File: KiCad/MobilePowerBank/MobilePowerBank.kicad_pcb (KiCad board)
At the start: 2 copper layers, 114 x 164 mm, 123 parts, among them J1 Power IN, J2 Power OUT, J3 Power OUT, J4 OLED I2C, J5 PDI, J6 OLED, J7 Power OUT, SW1 SW_DIP_x01, U1 INA169, U10 INA138, U2 LMZ14203H, U3 L78M12, U4 INA138, U5 UA78M33, U6 ATXMEGA32E5-AU, U7 LMZ14203H, U8 LMZ14203H, U9 INA138

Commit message: 5 power supplies created
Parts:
- removed the REF** at (134.6, 29.8)
- removed the REF** at (52.1, 29.8)
- added C45: 100u, Capacitors_Tantalum_SMD:CP_Tantalum_Case-V_EIA-7343-20_Wave, F.Cu at (46.4, 101.0)
- added C46: 100u, Capacitors_Tantalum_SMD:CP_Tantalum_Case-V_EIA-7343-20_Wave, F.Cu at (102.9, 101.0)
- added C47: 10u/35V/X7R, Capacitors_SMD:C_2220, F.Cu at (52.7, 101.0)
- added C48: 10u/35V/X7R, Capacitors_SMD:C_2220, F.Cu at (109.2, 101.0)
- added C49: 4u7, Capacitors_SMD:C_0805, F.Cu at (62.9, 109.2)
- added C50: 4u7, Capacitors_SMD:C_0805, F.Cu at (119.4, 109.2)
- added C51: 22n, Capacitors_SMD:C_0805, F.Cu at (70.5, 108.0)
- added C52: 22n, Capacitors_SMD:C_0805, F.Cu at (127.0, 108.0)
- added C53: 47u/1-45mESR, Capacitors_Tantalum_SMD:CP_Tantalum_Case-D_EIA-7343-31_Reflow, F.Cu at (70.5, 101.0)
- added C54: 47u/1-45mESR, Capacitors_Tantalum_SMD:CP_Tantalum_Case-D_EIA-7343-31_Reflow, F.Cu at (127.0, 101.0)
- added C55: 47u/1-45mESR, Capacitors_Tantalum_SMD:CP_Tantalum_Case-D_EIA-7343-31_Reflow, F.Cu at (76.2, 101.0)
- added C56: 47u/1-45mESR, Capacitors_Tantalum_SMD:CP_Tantalum_Case-D_EIA-7343-31_Reflow, F.Cu at (132.7, 101.0)
- added C57: 100n, Capacitors_SMD:C_0805, F.Cu at (8.87, 104.5)
- added C58: 100n, Capacitors_SMD:C_0805, F.Cu at (8.87, 100.8)
- added C59: 100n, Capacitors_SMD:C_0805, B.Cu at (80.0, 108.6)
- added C60: 100n, Capacitors_SMD:C_0805, B.Cu at (136.5, 108.6)
- added C61: 1u, Capacitors_SMD:C_0805, F.Cu at (25.6, 91.6)
- added C62: 1u, Capacitors_SMD:C_0805, F.Cu at (8.87, 102.6)
- added J8: Power OUT 4, Connectors_Terminal_Blocks:TerminalBlock_Altech_AK300-2_P5.00mm, F.Cu at (93.3, 103.5)
- added J9: Power OUT 5, Connectors_Terminal_Blocks:TerminalBlock_Altech_AK300-2_P5.00mm, F.Cu at (149.9, 103.5)
- added R56: 220k, Resistors_SMD:R_0805, F.Cu at (54.6, 108.6)
- added R57: 30k, Resistors_SMD:R_0805, F.Cu at (54.6, 110.5)
- added R58: 220k, Resistors_SMD:R_0805, F.Cu at (111.1, 108.6)
- added R59: 30k, Resistors_SMD:R_0805, F.Cu at (111.1, 110.5)
- added R60: 30k, Resistors_SMD:R_0805, F.Cu at (57.8, 108.6)
- added R61: 300k, Resistors_SMD:R_0805, F.Cu at (57.8, 110.5)
- added R62: 30k, Resistors_SMD:R_0805, F.Cu at (114.3, 108.6)
- added R63: 300k, Resistors_SMD:R_0805, F.Cu at (114.3, 110.5)
- added R64: 20k, Resistors_SMD:R_0805, F.Cu at (61.0, 111.1)
- added R65: 20k, Resistors_SMD:R_0805, F.Cu at (117.5, 111.1)
- added R66: 2k2, Resistors_SMD:R_0805, F.Cu at (66.0, 109.2)
- added R67: 2k2, Resistors_SMD:R_0805, F.Cu at (122.6, 109.2)
- added R68: 15k4, Resistors_SMD:R_0805, F.Cu at (67.9, 109.2)
- added R69: 15k4, Resistors_SMD:R_0805, F.Cu at (124.5, 109.2)
- added R70: 15k4, Resistors_SMD:R_0805, F.Cu at (70.5, 109.9)
- added R71: 15k4, Resistors_SMD:R_0805, F.Cu at (127.0, 109.9)
- added R72: 90k, Resistors_SMD:R_0805, F.Cu at (11.8, 108.2)
- added R73: 10k, Resistors_SMD:R_0805, F.Cu at (15.4, 104.5)
- added R74: 90k, Resistors_SMD:R_0805, F.Cu at (28.9, 91.6)
- added R75: 10k, Resistors_SMD:R_0805, F.Cu at (22.0, 95.8)
- added R76: 0R1, Resistors_SMD:R_2512, F.Cu at (83.2, 103.5)
- added R77: 0R1, Resistors_SMD:R_2512, F.Cu at (83.2, 107.3)
- added R78: 0R1, Resistors_SMD:R_2512, F.Cu at (83.2, 111.1)
- added R79: 0R1, Resistors_SMD:R_2512, F.Cu at (139.7, 103.5)
- added R80: 0R1, Resistors_SMD:R_2512, F.Cu at (139.7, 107.3)
- added R81: 0R1, Resistors_SMD:R_2512, F.Cu at (139.7, 111.1)
- added R82: 20k, Resistors_SMD:R_0805, B.Cu at (81.3, 111.8)
- added R83: 20k, Resistors_SMD:R_0805, B.Cu at (137.8, 111.8)
- added REF**: MountingHole_3.2mm_M3, Mounting_Holes:MountingHole_3.2mm_M3, F.Cu at (148.5, 188.5)
- added REF**: MountingHole_3.2mm_M3, Mounting_Holes:MountingHole_3.2mm_M3, F.Cu at (45.5, 188.5)
- added REF**: MountingHole_3.2mm_M3, Mounting_Holes:MountingHole_3.2mm_M3, F.Cu at (148.5, 55.5)
- added REF**: MountingHole_3.2mm_M3, Mounting_Holes:MountingHole_3.2mm_M3, F.Cu at (45.5, 55.5)
- added U11: LMZ14201H, TO_SOT_Packages_SMD:TO-263-7_TabPin4, F.Cu at (61.6, 98.4)
- added U12: LMZ14201H, TO_SOT_Packages_SMD:TO-263-7_TabPin4, F.Cu at (118.1, 98.4)
- added U13: INA138, TO_SOT_Packages_SMD:SOT-23-5, B.Cu at (83.2, 109.2)
- added U14: INA138, TO_SOT_Packages_SMD:SOT-23-5, B.Cu at (139.7, 109.2)
- added U15: ATXMEGA256A3U-AU, Housings_QFP:TQFP-64_14x14mm_Pitch0.8mm, B.Cu at (101.0, 31.1)
- J2: value Power OUT -> Power OUT 2
- J3: value Power OUT -> Power OUT 1
- J7: value Power OUT -> Power OUT 3
- moved REF** 148.0 mm to (236.1, 117.9)
- moved C27 143.3 mm to (179.1, 42.5)
- moved R24 114.3 mm to (132.1, 55.9), turned to 0 degrees
- moved C15 105.4 mm to (93.3, 50.8)
- moved C18 105.4 mm to (99.1, 66.7)
- moved C19 105.4 mm to (98.4, 66.7)
- moved C21 105.4 mm to (88.3, 56.5)
- moved C26 105.4 mm to (95.9, 50.8)
- moved L1 105.4 mm to (84.5, 56.5)
- moved R1 105.4 mm to (89.5, 50.8)
- moved R12 105.4 mm to (99.7, 50.8)
- moved R13 105.4 mm to (97.8, 50.8)
- moved R2 105.4 mm to (91.4, 50.8)
- moved U3 105.4 mm to (73.0, 56.5)
- moved C12 105.4 mm to (129.5, 48.3)
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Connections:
- C26 pad 1: OUT_Voltage -> OUT_1_Voltage
- C27 pad 1: OUT_Current -> OUT_1_Current
- C39 pad 1: OUT_Voltage -> OUT_2_Voltage
- C40 pad 1: OUT_Voltage -> OUT_3_Voltage
- C43 pad 1: OUT_Current -> OUT_2_Current
- C44 pad 1: OUT_Current -> OUT_3_Current
- R12 pad 2: OUT_Voltage -> OUT_1_Voltage
- R13 pad 1: OUT_Voltage -> OUT_1_Voltage
- R15 pad 1: OUT_Current -> OUT_1_Current
- R44 pad 2: OUT_Voltage -> OUT_2_Voltage
- R45 pad 1: OUT_Voltage -> OUT_2_Voltage
- R46 pad 2: OUT_Voltage -> OUT_3_Voltage
- R47 pad 1: OUT_Voltage -> OUT_3_Voltage
- R54 pad 1: OUT_Current -> OUT_2_Current
- R55 pad 1: OUT_Current -> OUT_3_Current
- U10 pad 1: OUT_Current -> OUT_3_Current
- U4 pad 1: OUT_Current -> OUT_1_Current
- U6 pad 5: OUT_Voltage -> (no net)
- U6 pad 6: OUT_Current -> (no net)
- U9 pad 1: OUT_Current -> OUT_2_Current
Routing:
- net GNDA: track 198.0 -> 309.8 mm
- net POWER_IN: track 165.2 -> 120.5 mm
- net OUT_Current: track 41.5 -> 0.00 mm, vias 1 -> 0
- net Net-(C52-Pad1): track 0.00 -> 29.5 mm
- net Net-(C51-Pad1): track 0.00 -> 28.5 mm
- net IN_Current: track 38.8 -> 11.1 mm
- net PDI_CLK: track 44.0 -> 17.6 mm
- net PDI_DATA: track 41.7 -> 22.7 mm
- net Net-(C10-Pad1): track 65.5 -> 48.5 mm
- net GND: track 275.4 -> 258.5 mm, vias 9 -> 8
- net (no net): track 1.90 -> 17.7 mm, vias 0 -> 1
- net Net-(F1-Pad1): track 15.0 -> 0.00 mm
- net Net-(C52-Pad2): track 0.00 -> 8.61 mm
- net Net-(C51-Pad2): track 0.00 -> 8.61 mm
- net Net-(R63-Pad2): track 0.00 -> 8.31 mm
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- added copper zone on F.Cu, net Net-(C51-Pad1)
- added copper zone on F.Cu, net Net-(C52-Pad1)
- added copper zone on F.Cu, net POWER_4_OUT
- added copper zone on F.Cu, net POWER_5_OUT
- removed copper zone on B.Cu, net Net-(F1-Pad1)
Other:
- board text removed: "In(35V)"
- board text removed: "Out"
- board text removed: "Vin"
- board text removed: "Vout"

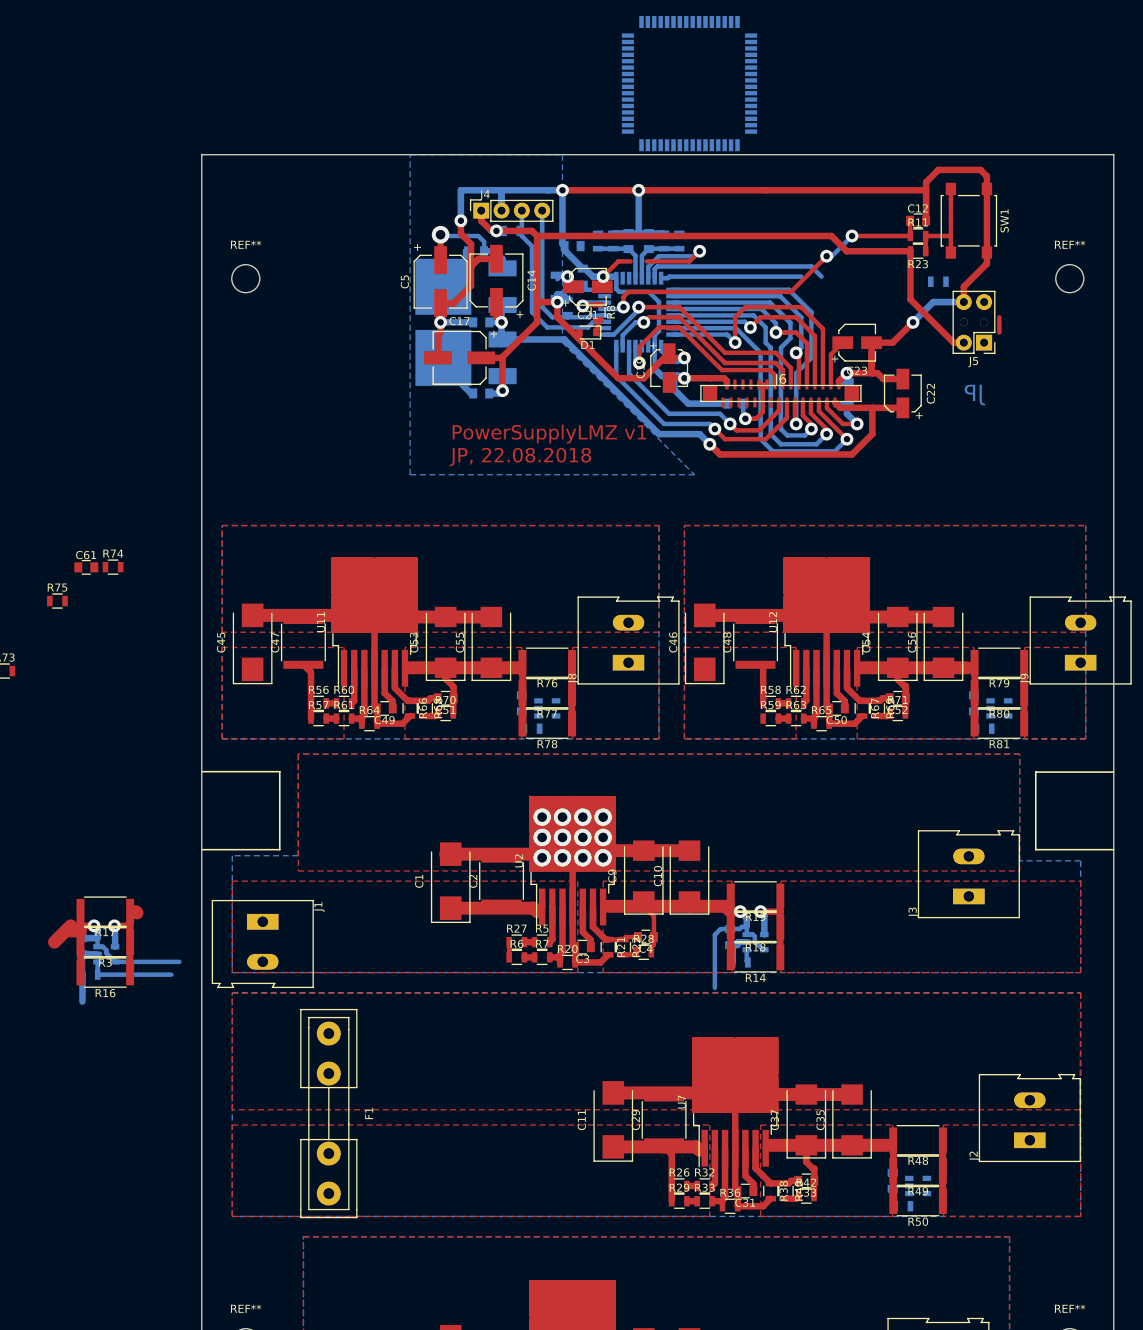
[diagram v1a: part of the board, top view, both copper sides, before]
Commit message: xmega added
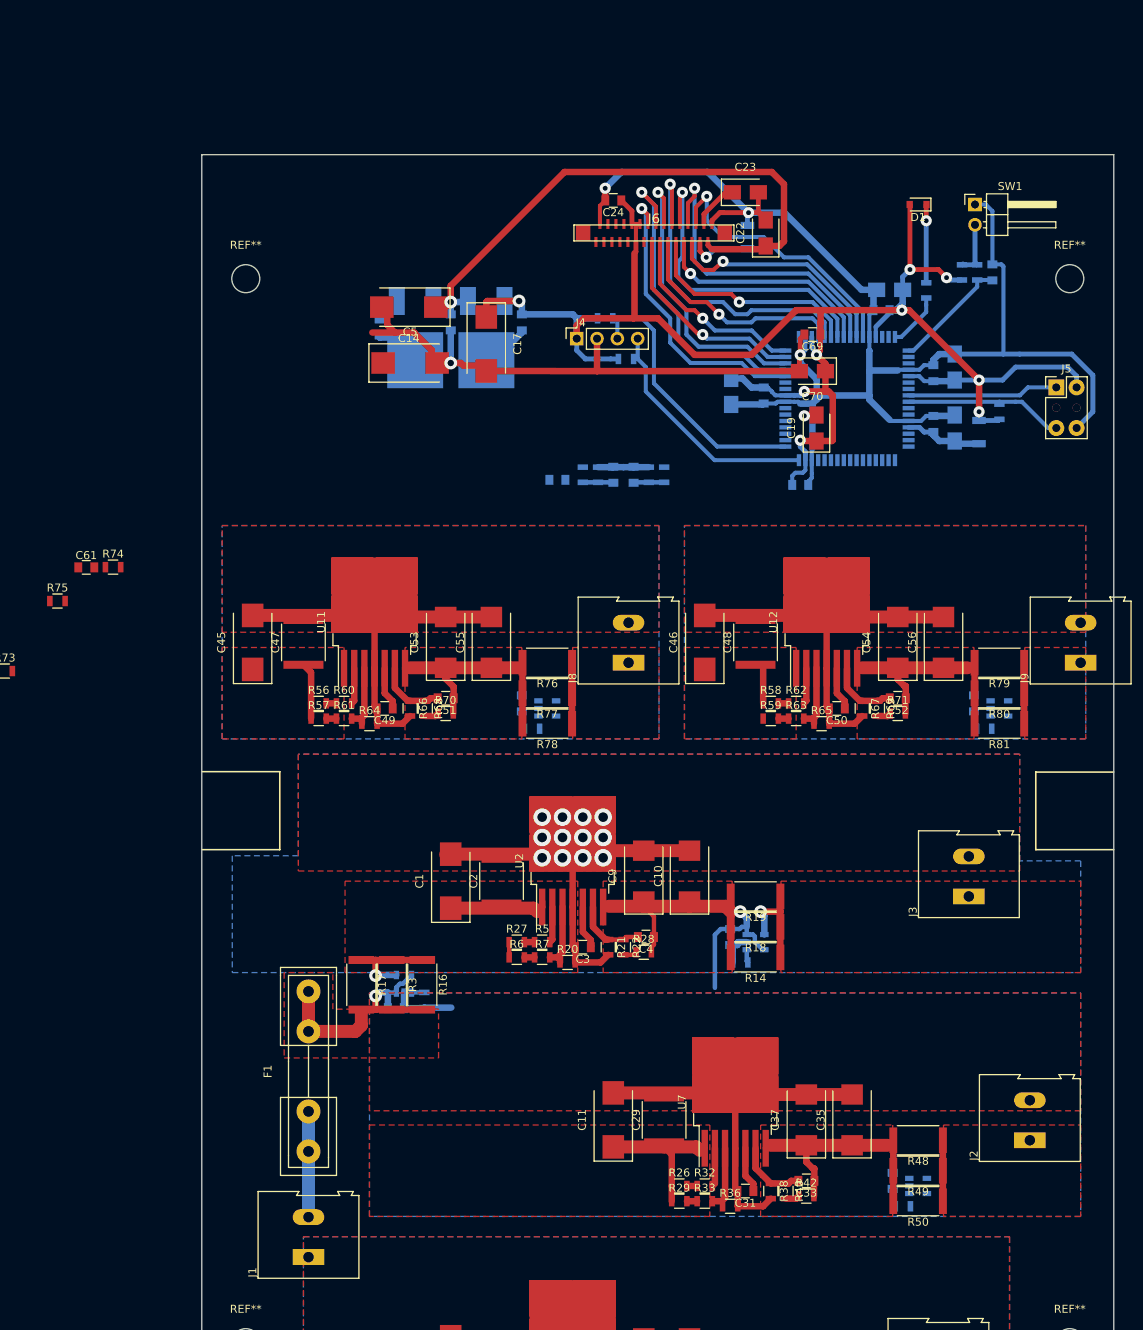
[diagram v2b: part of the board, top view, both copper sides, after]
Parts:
- removed U6: ATXMEGA32E5-AU, Housings_QFP:TQFP-32_7x7mm_Pitch0.8mm
- added C63: 100n, Capacitors_SMD:C_0805, B.Cu at (125.0, 59.4)
- added C64: 10u, Capacitors_Tantalum_SMD:CP_Tantalum_Case-B_EIA-3528-21_Wave, B.Cu at (126.0, 56.9)
- added C65: 100n, Capacitors_SMD:C_0805, B.Cu at (131.4, 67.3)
- added C66: 10u, Capacitors_Tantalum_SMD:CP_Tantalum_Case-B_EIA-3528-21_Wave, B.Cu at (134.1, 66.5)
- added C67: 100n, Capacitors_SMD:C_0805, B.Cu at (110.2, 70.1)
- added C68: 10u, Capacitors_Tantalum_SMD:CP_Tantalum_Case-B_EIA-3528-21_Wave, B.Cu at (106.2, 69.6)
- added C69: 100n, Capacitors_SMD:C_0805, F.Cu at (116.3, 62.5)
- added C70: 10u, Capacitors_Tantalum_SMD:CP_Tantalum_Case-B_EIA-3528-21_Wave, F.Cu at (116.3, 67.1)
- C1, C11, C28, C45, C46: value 100u -> 47u
- C12, R11, R23, R8: moved to B.Cu
- C13: value 100n -> 47u
- C14: footprint Capacitors_SMD:CP_Elec_6.3x7.7 -> Capacitors_Tantalum_SMD:CP_Tantalum_Case-V_EIA-7343-20_Wave
- C17: footprint Capacitors_SMD:CP_Elec_6.3x5.8 -> Capacitors_Tantalum_SMD:CP_Tantalum_Case-V_EIA-7343-20_Wave
- C19, C22, C23: footprint Capacitors_SMD:CP_Elec_4x5.8 -> Capacitors_Tantalum_SMD:CP_Tantalum_Case-B_EIA-3528-21_Wave
- C21: footprint Capacitors_SMD:CP_Elec_4x5.8 -> Capacitors_Tantalum_SMD:CP_Tantalum_Case-B_EIA-3528-21_Wave; moved to B.Cu
- C24: moved to F.Cu
- C5: value 100u -> 47u; footprint Capacitors_SMD:CP_Elec_6.3x7.7 -> Capacitors_Tantalum_SMD:CP_Tantalum_Case-V_EIA-7343-20_Wave
- SW1: footprint Buttons_Switches_SMD:SW_SPST_B3S-1000 -> Pin_Headers:Pin_Header_Angled_1x02_Pitch2.54mm
- moved L1 55.7 mm to (137.2, 74.7), turned to 270 degrees
- moved C21 49.1 mm to (134.1, 74.2), turned to 90 degrees
- moved C20 47.5 mm to (131.4, 73.7)
- moved D1 44.3 mm to (129.5, 46.2)
- moved U15 44.0 mm to (120.7, 70.5), turned to 90 degrees
- moved J1 42.3 mm to (53.3, 177.8), turned to 90 degrees
- moved R4 41.9 mm to (67.8, 145.7), turned to 270 degrees
- moved R8 41.1 mm to (130.6, 57.0), turned to 90 degrees
- moved C7 40.0 mm to (64.3, 146.7), turned to 180 degrees
- moved R16 39.7 mm to (67.6, 143.8), turned to 270 degrees
- moved U1 37.4 mm to (65.3, 143.6), turned to 90 degrees
- moved R3 36.2 mm to (63.8, 143.8), turned to 270 degrees
- moved R17 33.3 mm to (59.9, 143.8), turned to 270 degrees
- moved C24 29.6 mm to (91.4, 45.7)
- moved C15 29.3 mm to (91.4, 80.0)
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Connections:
- C7 pad 2: POWER_IN -> VDD
- F1 pad 2: POWER_IN -> VDD
- R1 pad 1: POWER_IN -> VDD
- R16 pad 2: POWER_IN -> VDD
- R17 pad 2: POWER_IN -> VDD
- R3 pad 2: POWER_IN -> VDD
- U1 pad 3: POWER_IN -> VDD
- U1 pad 5: POWER_IN -> VDD
- U15 pad 14: (no net) -> GND
- U15 pad 15: (no net) -> +3V3
- U15 pad 16: (no net) -> SDA
- U15 pad 17: (no net) -> SCK
- U15 pad 24: (no net) -> GND
- U15 pad 25: (no net) -> +3V3
- U15 pad 28: (no net) -> /OLED_!DS
- U15 pad 29: (no net) -> /OLED_D/!C
- U15 pad 30: (no net) -> /OLED_E/!RD
- U15 pad 31: (no net) -> /OLED_!RES
- U15 pad 32: (no net) -> /OLED_R/!W
- U15 pad 34: (no net) -> GND
- U15 pad 35: (no net) -> +3V3
- U15 pad 36: (no net) -> /OLED_D0
- U15 pad 37: (no net) -> /OLED_D1
- U15 pad 38: (no net) -> /OLED_D2
- U15 pad 39: (no net) -> /OLED_D3
- U15 pad 40: (no net) -> /OLED_D4
- U15 pad 41: (no net) -> /OLED_D5
- U15 pad 42: (no net) -> /OLED_D6
- U15 pad 43: (no net) -> /OLED_D7
- U15 pad 44: (no net) -> GND
- U15 pad 45: (no net) -> +3V3
- U15 pad 48: (no net) -> LED
- U15 pad 49: (no net) -> SWITCH
- U15 pad 52: (no net) -> GND
- U15 pad 53: (no net) -> +3V3
- U15 pad 56: (no net) -> PDI_DATA
- U15 pad 57: (no net) -> PDI_CLK
- U15 pad 60: (no net) -> GND
- U15 pad 61: (no net) -> /+3.3VA
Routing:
- net +3V3: track 142.3 -> 210.9 mm, vias 5 -> 9
- net POWER_IN: track 120.5 -> 79.8 mm, vias 3 -> 1
- net GND: track 258.5 -> 297.5 mm, vias 8 -> 5
- net VDD: track 0.00 -> 31.3 mm, vias 0 -> 1
- net SWITCH: track 44.7 -> 14.7 mm, vias 3 -> 0
- net (no net): track 17.7 -> 0.00 mm, vias 1 -> 0
- net /OLED_D1: track 26.0 -> 40.9 mm
- net /OLED_D3: track 24.4 -> 39.2 mm
- net /OLED_D5: track 25.6 -> 38.9 mm
- net Net-(F1-Pad1): track 0.00 -> 13.2 mm
- net /OLED_D/!C: track 26.9 -> 39.9 mm
- net /OLED_D6: track 41.2 -> 29.3 mm
- net /OLED_D2: track 39.5 -> 27.9 mm
- net SCK: track 23.4 -> 34.6 mm
- net /OLED_!DS: track 25.9 -> 36.6 mm
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- added copper zone on F.Cu, net VDD
- removed copper zone on B.Cu, net GND
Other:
- net class Default: trace_width 0.8128 -> 0.6096; via_dia 1.6 -> 1.4; via_drill 0.8 -> 0.6
- net class Signal added: clearance 0.2032, trace_width 0.508, via_dia 1.4, via_drill 0.6
- board text removed: "JP"
- board text removed: "PowerSupplyLMZ v1 JP, 22.08.2018"
